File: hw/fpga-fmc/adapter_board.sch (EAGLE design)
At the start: 115 parts, among them IC1 M24C02, J1 5569262-1, J2 ASP-134488-01, U1 ADM3066E, U10 ADM3066E, U11 ADM3066E, U12 ADM3066E, U13 ADM3066E, U14 ADM3066E, U15 ADM3066E, U16 ADM3066E, U17 TCA9548A, U2 ADM3066E, U3 ADM3066E, U4 ADM3066E, U5 ADM3066E, U6 ADM3066E, U7 ADM3066E, U8 ADM3066E, U9 ADM3066E

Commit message: fpga-fmc: route right side
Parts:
- removed R54: (no value), rcl:R-EU_R0805
- added U$4: TXS0102, parts:TXS0102
- U$2: value TXS0104E -> TXS0102; device parts:TXS0104E -> parts:TXS0102
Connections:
- removed net N$13: R54.2, U$2.OE
- removed net N$2: U$2.A4
- removed net N$3: U$2.A3
- removed net N$4: U$2.A2
- removed net N$5: U$2.A1
- new net FMC_HA00_CC_N: J2E.F5, R23.2
- new net FMC_HA00_CC_P: J2E.F4, U2.DE, U2.RE
- new net FMC_HA01_CC_N: J2D.E3, U1.DE, U1.RE
- new net FMC_HA01_CC_P: J2D.E2, R2.2
- net 0V: now also U$4.GND; no longer R54.1
- net 1V8: now also U$4.VCCA
- net 5V: now also U$4.VCCB
- net CONV_OE: now also U$2.OE, U$4.OE
- net FMC_DP0_C2M_N: now also R25.2; no longer U1.DE, U1.RE
- net FMC_DP0_C2M_P: now also U3.DE, U3.RE; no longer R2.2
- net FMC_DP0_M2C_N: now also R29.2; no longer R27.2
- net FMC_DP0_M2C_P: now also U5.DE, U5.RE; no longer U4.DE, U4.RE
- net FMC_LA00_CC_N: now also R27.2; no longer R23.2
- net FMC_LA00_CC_P: now also U4.DE, U4.RE; no longer U2.DE, U2.RE
- net FMC_LA01_CC_N: now also R35.2; no longer R31.2
- net FMC_LA01_CC_P: now also U8.DE, U8.RE; no longer U6.DE, U6.RE
- net FMC_LA02_N: now also U$1.A1; no longer R25.2
- net FMC_LA02_P: now also U$1.A2; no longer U3.DE, U3.RE
- net FMC_LA03_N: now also U$3.A1; no longer R29.2
- net FMC_LA03_P: now also U$3.A2; no longer U5.DE, U5.RE
- net FMC_LA04_N: now also R31.2; no longer U$1.A1
- net FMC_LA04_P: now also U6.DE, U6.RE; no longer U$1.A2
- net FMC_LA05_N: now also R6.1, U17.SCL; no longer R35.2
- net FMC_LA05_P: now also R5.1, U17.SDA; no longer U8.DE, U8.RE
- net FMC_LA07_N: now also R51.2; no longer R39.2
- net FMC_LA07_P: now also U16.DE, U16.RE; no longer U10.DE, U10.RE
- net FMC_LA08_N: now also U$2.A1; no longer U$3.A1
- net FMC_LA08_P: now also U$2.A2; no longer U$3.A2
- net FMC_LA09_N: now also R39.2; no longer R37.2
- net FMC_LA09_P: now also U10.DE, U10.RE; no longer U9.DE, U9.RE
- net FMC_LA10_N: now also R37.2; no longer R6.1, U17.SCL
- net FMC_LA10_P: now also U9.DE, U9.RE; no longer R5.1, U17.SDA
- net FMC_LA11_N: now also R49.2; no longer R51.2
- net FMC_LA11_P: now also U15.DE, U15.RE; no longer U16.DE, U16.RE
- net FMC_LA12_N: now also U$4.A1; no longer R45.2
- net FMC_LA12_P: now also U$4.A2; no longer U13.DE, U13.RE
- net FMC_LA15_N: now also R47.2; no longer R49.2
- net FMC_LA15_P: now also U14.DE, U14.RE; no longer U15.DE, U15.RE
- net FMC_LA16_N: now also R45.2; no longer R47.2
- net FMC_LA16_P: now also U13.DE, U13.RE; no longer U14.DE, U14.RE
- net RJ1_CONV: now also U$4.B1; no longer U$2.B4
- net RJ5_CONV: now also U$4.B2; no longer U$2.B3

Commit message: hw/fpga-fmc: add 5V supply and route remaining CONV signals
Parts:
- added U$5: TSR1, parts:TSR1
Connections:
- net +12V: now also U$5.VIN; no longer J1.1.4, J1.2.4, J1.3.4, J1.4.4, J1.5.4, J1.6.4, J1.7.4, J1.8.4
- net 0V: now also U$5.GND+
- net 5V: now also J1.1.4, J1.2.4, J1.3.4, J1.4.4, J1.5.4, J1.6.4, J1.7.4, J1.8.4, U$5.VOUT
- net RJ1_CLK_N: now also R44.2, U13.B; no longer R48.2, U15.B
- net RJ1_CLK_P: now also R44.1, U13.A; no longer R48.1, U15.A
- net RJ1_DATA_N: now also R46.2, U14.B; no longer R50.2, U16.B
- net RJ1_DATA_P: now also R46.1, U14.A; no longer R50.1, U16.A
- net RJ2_CLK_N: now also R36.2, U9.B; no longer R40.2, U11.B
- net RJ2_CLK_P: now also R36.1, U9.A; no longer R40.1, U11.A
- net RJ2_DATA_N: now also R38.2, U10.B; no longer R42.2, U12.B
- net RJ2_DATA_P: now also R38.1, U10.A; no longer R42.1, U12.A
- net RJ5_CLK_N: now also R48.2, U15.B; no longer R44.2, U13.B
- net RJ5_CLK_P: now also R48.1, U15.A; no longer R44.1, U13.A
- net RJ5_DATA_N: now also R50.2, U16.B; no longer R46.2, U14.B
- net RJ5_DATA_P: now also R50.1, U16.A; no longer R46.1, U14.A
- net RJ6_CLK_N: now also R40.2, U11.B; no longer R36.2, U9.B
- net RJ6_CLK_P: now also R40.1, U11.A; no longer R36.1, U9.A
- net RJ6_DATA_N: now also R42.2, U12.B; no longer R38.2, U10.B
- net RJ6_DATA_P: now also R42.1, U12.A; no longer R38.1, U10.A

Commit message: hw/fpga-fmc: finalize pcb design and prepare BOM
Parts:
- removed U$5: TSR1, parts:TSR1
- added 12V_GOOD, 3V3_GOOD2, 5V_GOOD: (no value), led:LEDCHIPLED_0805
- added EESCL, EESDA, M_SCL, M_SDA, RJ1_CL+, RJ1_CL-, RJ1_CONV, RJ1_FC, RJ1_FCD, RJ1_FCL, RJ1_FDA, RJ1_FDA+, RJ1_FDA-, RJ1_FDD, RJ1_SCL, RJ1_SDO, RJ2_CONV, RJ2_FC, RJ2_FCD, RJ2_FCL, RJ2_FCL+, RJ2_FCL-, RJ2_FDA, RJ2_FDA+, RJ2_FDA-, RJ2_FDD, RJ2_SCL, RJ2_SDO, RJ3_CONV, RJ3_FC, RJ3_FCD, RJ3_FCL, RJ3_FCL+, RJ3_FCL-, RJ3_FDA, RJ3_FDA+, RJ3_FDA-, RJ3_FDD, RJ3_SCL, RJ3_SDO: TPB1,27, testpad:TPB1,27
- added J3, J4: (no value), pinhead:PINHD-1X3
- added R53: 330R, resistor:R-EU_R0805
- added R54: 1k, resistor:R-EU_R0805
- added R56: 130R, resistor:R-EU_R0805
- added R57, R58: 0R, rcl:R-EU_R0805
- added R59: NB, rcl:R-EU_R0805
- added X1: (no value), con-wago-508:W237-02P
- R1, R22, R24, R26, R28, R30, R32, R34, R36, R38, R40, R42, R44, R46, R48, R50: value (none) -> 120R
- R10, R11, R12, R13, R14, R15, R16, R17, R18, R19, R20, R21, R3, R4, R5, R6, R8, R9: value 1k -> 4k
- R55: value (none) -> 10k
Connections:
- new net FMC_HA05_N: J2D.E7, R59.1, U$1.A1
- new net N$2: 12V_GOOD.C, R54.2
- new net N$3: 3V3_GOOD2.C, R56.2
- new net N$5: 5V_GOOD.C, R53.2
- net +12V: now also 12V_GOOD.A, J3.2; no longer U$5.VIN
- net +3V3: now also 3V3_GOOD2.A, J3.1
- net 0V: now also J3.3, J4.3, R53.1, R54.1, R56.1, R59.2, X1-1.KL; no longer U$5.GND+
- net 1V8: now also J4.2
- net 1V8_POWER_GOOD: now also R58.1
- net 5V: now also 5V_GOOD.A, X1-2.KL; no longer U$5.VOUT
- net CONV_OE: now also R57.1, R58.2
- net FMC_IIC_SCL: now also EESCL.TP
- net FMC_IIC_SDA: now also EESDA.TP
- net FMC_LA01_CC_N: now also RJ3_FDA.TP
- net FMC_LA01_CC_P: now also RJ3_FDD.TP
- net FMC_LA02_N: now also R57.2; no longer U$1.A1
- net FMC_LA03_P: now also RJ3_FC.TP
- net FMC_LA05_N: now also M_SCL.TP
- net FMC_LA05_P: now also M_SDA.TP
- net FMC_LA06_N: now also RJ3_FCL.TP
- net FMC_LA06_P: now also RJ3_FCD.TP
- net FMC_LA08_N: now also RJ2_FC.TP
- net FMC_LA09_N: now also RJ2_FDA.TP
- net FMC_LA09_P: now also RJ2_FDD.TP
- net FMC_LA10_N: now also RJ2_FCL.TP
- net FMC_LA10_P: now also RJ2_FCD.TP
- net FMC_LA12_N: now also RJ1_FC.TP
- net FMC_LA15_N: now also RJ1_FDA.TP
- net FMC_LA15_P: now also RJ1_FDD.TP
- net FMC_LA16_N: now also RJ1_FCL.TP
- net FMC_LA16_P: now also RJ1_FCD.TP
- net RJ1_CLK_N: now also RJ1_CL-.TP
- net RJ1_CLK_P: now also RJ1_CL+.TP
- net RJ1_CONV: now also RJ1_CONV.TP
- net RJ1_DATA_N: now also RJ1_FDA-.TP
- net RJ1_DATA_P: now also RJ1_FDA+.TP
- net RJ1_SCL: now also RJ1_SCL.TP
- net RJ1_SDO: now also RJ1_SDO.TP
- net RJ2_CLK_N: now also RJ2_FCL-.TP
- net RJ2_CLK_P: now also RJ2_FCL+.TP
- net RJ2_CONV: now also RJ2_CONV.TP
- net RJ2_DATA_N: now also RJ2_FDA-.TP
- net RJ2_DATA_P: now also RJ2_FDA+.TP
- net RJ2_SCL: now also RJ2_SCL.TP
- net RJ2_SDO: now also RJ2_SDO.TP
- net RJ3_CLK_N: now also RJ3_FCL-.TP
- net RJ3_CLK_P: now also RJ3_FCL+.TP
- net RJ3_CONV: now also RJ3_CONV.TP
- net RJ3_DATA_N: now also RJ3_FDA-.TP
- net RJ3_DATA_P: now also RJ3_FDA+.TP
- net RJ3_SCL: now also RJ3_SCL.TP
- net RJ3_SDO: now also RJ3_SDO.TP
- net V+: now also J4.1
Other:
- moved on the sheet: C35, C36, C37

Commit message: hw/fpga-fmc: fix clearance issues
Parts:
- IC1: device parts:N24C02UDTG -> parts:N24C02UDTGSO8N
- R10, R11, R12, R13, R14, R15, R16, R17, R18, R19, R20, R21, R3, R4, R5, R6, R8, R9: value 4k -> 4.7k
- R52: value 0R -> NB
- renumbered 3V3_GOOD2 to 3V3_GOOD, U$1 to U18, U$2 to U20, U$3 to U19, U$4 to U21

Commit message: hw/fpga-fmc: fix connector turned by 180 degrees. add led for 1v8. change i2c package
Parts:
- added 1V8_GOOD: (no value), led:LEDCHIPLED_0805
- added R60: 10R, resistor:R-EU_R0805
- added R61: 10k, resistor:R-EU_R0805
- added R62: 130R, resistor:R-EU_R0805
- added U40: IRLML2502, parts:IRLML2502
- IC1: device parts:N24C02UDTGSO8N -> parts:N24C02UDTGTSSOP8
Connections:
- new net N$6: R60.1, R61.1, U40.G
- new net N$8: R62.2, U40.D
- new net N$9: 1V8_GOOD.C, R62.1
- net +3V3: now also 1V8_GOOD.A
- net 0V: now also R61.2, U40.S, X1-2.KL; no longer U17.A0, U17.A1, X1-1.KL
- net 1V8: now also R60.2
- net 5V: now also X1-1.KL; no longer X1-2.KL
- net FMC_IIC_SCL: now also M_SCL.TP, R6.1, U17.SCL
- net FMC_IIC_SDA: now also M_SDA.TP, R5.1, U17.SDA
- net FMC_LA05_N: no longer M_SCL.TP, R6.1, U17.SCL
- net FMC_LA05_P: no longer M_SDA.TP, R5.1, U17.SDA
- net GA0: now also U17.A1
- net GA1: now also U17.A0
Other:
- moved on the sheet: X1-1, X1-2

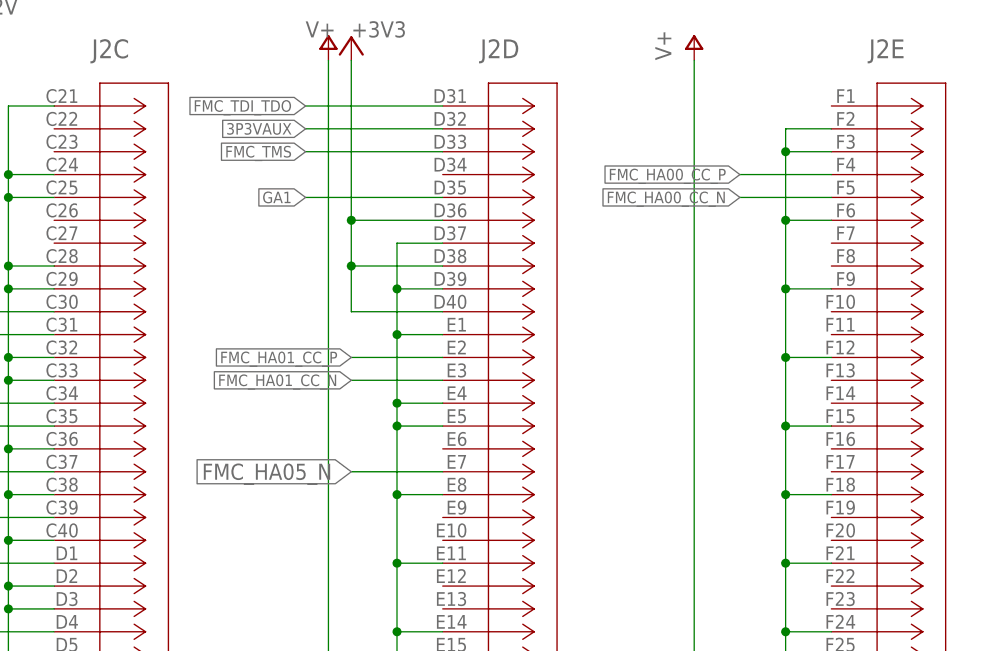
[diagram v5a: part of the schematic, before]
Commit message: hdl: copy all pin assignments to constraint file
note: RJ8 FMC connection are not connected on the FPGA board, so RJ8 cannot be used with the prototype pcb
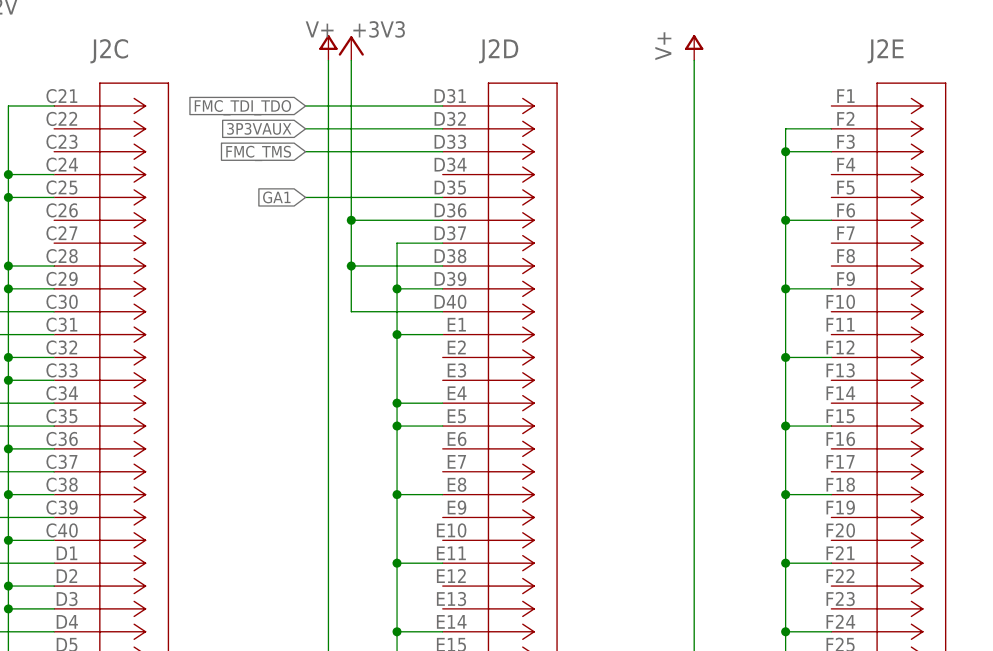
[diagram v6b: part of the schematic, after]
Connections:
- net FMC_HA00_CC_N: no longer J2E.F5
- net FMC_HA00_CC_P: no longer J2E.F4
- net FMC_HA01_CC_N: no longer J2D.E3
- net FMC_HA01_CC_P: no longer J2D.E2
- net FMC_HA05_N: no longer J2D.E7
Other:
- note added: "DO NOT CONNECT RJ8 TO HA PORTS!"
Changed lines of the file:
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@@
 <text x="1056.64" y="-25.4" size="1.778" layer="97">DATA IO 5</text>
 <text x="-279.4" y="104.14" size="1.27" layer="97">According to https://ohwr.org/project/ed/wikis/schematics-checklist#fmc-mezzanine-cards</text>
+<text x="-160.02" y="30.48" size="6.4516" layer="88">DO NOT CONNECT RJ8 TO HA PORTS!</text>
 </plain>
 <instances>
@@
 <net name="FMC_HA01_CC_P" class="0">
 <segment>
-<pinref part="J2" gate="D" pin="E2"/>
-<wire x1="-40.64" y1="287.02" x2="-50.8" y2="287.02" width="0.1524" layer="91"/>
-<label x="-50.8" y="287.02" size="1.27" layer="95" rot="R180" xref="yes"/>
-</segment>
-<segment>
 <pinref part="R2" gate="G$1" pin="2"/>
 <wire x1="149.86" y1="7.62" x2="147.32" y2="7.62" width="0.1524" layer="91"/>
@@
 <net name="FMC_HA01_CC_N" class="0">
 <segment>
-<pinref part="J2" gate="D" pin="E3"/>
-<wire x1="-40.64" y1="284.48" x2="-50.8" y2="284.48" width="0.1524" layer="91"/>
-<label x="-50.8" y="284.48" size="1.27" layer="95" rot="R180" xref="yes"/>
-</segment>
-<segment>
 <wire x1="154.94" y1="2.54" x2="147.32" y2="2.54" width="0.1524" layer="91"/>
 <pinref part="U1" gate="G$1" pin="DE"/>
@@
 <net name="FMC_HA00_CC_P" class="0">
 <segment>
-<pinref part="J2" gate="E" pin="F4"/>
-<wire x1="2.54" y1="307.34" x2="-7.62" y2="307.34" width="0.1524" layer="91"/>
-<label x="-7.62" y="307.34" size="1.27" layer="95" rot="R180" xref="yes"/>
-</segment>
-<segment>
 <wire x1="154.94" y1="-53.34" x2="147.32" y2="-53.34" width="0.1524" layer="91"/>
 <pinref part="U2" gate="G$1" pin="DE"/>
@@
 <net name="FMC_HA00_CC_N" class="0">
 <segment>
-<pinref part="J2" gate="E" pin="F5"/>
-<wire x1="2.54" y1="304.8" x2="-7.62" y2="304.8" width="0.1524" layer="91"/>
-<label x="-7.62" y="304.8" size="1.27" layer="95" rot="R180" xref="yes"/>
-</segment>
-<segment>
 <pinref part="R23" gate="G$1" pin="2"/>
 <wire x1="149.86" y1="-48.26" x2="147.32" y2="-48.26" width="0.1524" layer="91"/>
@@
 <net name="FMC_HA05_N" class="0">
 <segment>
-<pinref part="J2" gate="D" pin="E7"/>
-<wire x1="-40.64" y1="274.32" x2="-50.8" y2="274.32" width="0.1524" layer="91"/>
-<label x="-50.8" y="274.32" size="1.778" layer="95" rot="R180" xref="yes"/>
-</segment>
-<segment>
 <pinref part="U18" gate="G$1" pin="A1"/>

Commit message: turn FMC connector and reroute signals
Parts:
- added R63, R64: 0R, rcl:R-EU_R0805
- added R65, R66: 0R DNP, rcl:R-EU_R0805
- R57: value 0R -> 0R DNP
- R59: value NB -> DNP
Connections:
- removed net FMC_HA00_CC_N: R23.2
- removed net FMC_HA00_CC_P: U2.DE, U2.RE
- removed net FMC_HA01_CC_N: U1.DE, U1.RE
- removed net FMC_HA01_CC_P: R2.2
- removed net FMC_HA05_N: R59.1, U18.A1
- removed net I2C_RESET: R7.1, U17.RESET
- new net FMC_LA17_CC_N: J2C.D21
- new net FMC_LA17_CC_P: J2C.D20
- new net FMC_LA18_CC_N: J2C.C23
- new net FMC_LA18_CC_P: J2C.C22
- new net FMC_LA19_N: J2G.H23, RJ3_FC.TP, U19.A2
- new net FMC_LA19_P: J2G.H22, U19.A1
- new net FMC_LA20_N: J2F.G22
- new net FMC_LA20_P: J2F.G21
- new net FMC_LA21_N: J2G.H26, RJ3_FDD.TP, U8.DE, U8.RE
- new net FMC_LA21_P: J2G.H25, R35.2, RJ3_FDA.TP
- new net FMC_LA22_N: J2F.G25, R57.2
- new net FMC_LA22_P: J2F.G24, R7.1, U17.RESET
- new net FMC_LA23_N: J2C.D24
- new net FMC_LA23_P: J2C.D23
- new net FMC_LA24_N: J2G.H29, U6.DE, U6.RE
- new net FMC_LA24_P: J2G.H28, R31.2
- new net FMC_LA25_N: J2F.G28, RJ3_FCD.TP, U7.DE, U7.RE
- new net FMC_LA25_P: J2F.G27, R33.2, RJ3_FCL.TP
- new net FMC_LA26_N: J2C.D27
- new net FMC_LA26_P: J2C.D26
- new net FMC_LA27_N: J2C.C27
- new net FMC_LA27_P: J2C.C26
- new net FMC_LA28_N: J2G.H32, U5.DE, U5.RE
- new net FMC_LA28_P: J2G.H31, R29.2
- new net FMC_LA29_N: J2F.G31, U18.A2
- new net FMC_LA29_P: J2F.G30, R59.1, U18.A1
- new net FMC_LA30_N: J2G.H35, U4.DE, U4.RE
- new net FMC_LA30_P: J2G.H34, R27.2
- new net FMC_LA31_N: J2F.G34, R25.2
- new net FMC_LA31_P: J2F.G33, U3.DE, U3.RE
- new net FMC_LA32_N: J2G.H38, U2.DE, U2.RE
- new net FMC_LA32_P: J2G.H37, R23.2
- new net FMC_LA33_N: J2F.G37, U1.DE, U1.RE
- new net FMC_LA33_P: J2F.G36, R2.2
- new net I2C_SCL: M_SCL.TP, R6.1, R64.2, R66.1, U17.SCL
- new net I2C_SDA: M_SDA.TP, R5.1, R63.2, R65.1, U17.SDA
- net FMC_DP0_C2M_N: no longer R25.2
- net FMC_DP0_C2M_P: no longer U3.DE, U3.RE
- net FMC_DP0_M2C_N: no longer R29.2
- net FMC_DP0_M2C_P: no longer U5.DE, U5.RE
- net FMC_IIC_SCL: now also R64.1; no longer M_SCL.TP, R6.1, U17.SCL
- net FMC_IIC_SDA: now also R63.1; no longer M_SDA.TP, R5.1, U17.SDA
- net FMC_LA00_CC_N: now also RJ1_FCD.TP, U13.DE, U13.RE; no longer R27.2
- net FMC_LA00_CC_P: now also R45.2, RJ1_FCL.TP; no longer U4.DE, U4.RE
- net FMC_LA01_CC_N: now also R51.2; no longer R35.2, RJ3_FDA.TP
- net FMC_LA01_CC_P: now also U16.DE, U16.RE; no longer RJ3_FDD.TP, U8.DE, U8.RE
- net FMC_LA02_N: now also U21.A2; no longer R57.2
- net FMC_LA02_P: now also RJ1_FC.TP, U21.A1; no longer U18.A2
- net FMC_LA03_N: now also U12.DE, U12.RE; no longer U19.A1
- net FMC_LA03_P: now also R43.2; no longer RJ3_FC.TP, U19.A2
- net FMC_LA04_N: now also U11.DE, U11.RE; no longer R31.2
- net FMC_LA04_P: now also R41.2; no longer U6.DE, U6.RE
- net FMC_LA05_N: now also RJ1_FDD.TP, U14.DE, U14.RE
- net FMC_LA05_P: now also R47.2, RJ1_FDA.TP
- net FMC_LA06_N: now also U15.DE, U15.RE; no longer R33.2, RJ3_FCL.TP
- net FMC_LA06_P: now also R49.2; no longer RJ3_FCD.TP, U7.DE, U7.RE
- net FMC_LA07_N: now also RJ2_FDD.TP, U10.DE, U10.RE; no longer R51.2
- net FMC_LA07_P: now also R39.2, RJ2_FDA.TP; no longer U16.DE, U16.RE
- net FMC_LA08_N: no longer RJ2_FC.TP, U20.A1
- net FMC_LA08_P: no longer U20.A2
- net FMC_LA09_N: no longer R39.2, RJ2_FDA.TP
- net FMC_LA09_P: no longer RJ2_FDD.TP, U10.DE, U10.RE
- net FMC_LA10_N: no longer R37.2, RJ2_FCL.TP
- net FMC_LA10_P: no longer RJ2_FCD.TP, U9.DE, U9.RE
- net FMC_LA11_N: now also RJ2_FCD.TP, U9.DE, U9.RE; no longer R49.2
- net FMC_LA11_P: now also R37.2, RJ2_FCL.TP; no longer U15.DE, U15.RE
- net FMC_LA12_N: no longer RJ1_FC.TP, U21.A1
- net FMC_LA12_P: no longer U21.A2
- net FMC_LA13_N: no longer R43.2
- net FMC_LA13_P: no longer U12.DE, U12.RE
- net FMC_LA14_N: now also R65.2; no longer R41.2
- net FMC_LA14_P: now also R66.2; no longer U11.DE, U11.RE
- net FMC_LA15_N: now also U20.A2; no longer R47.2, RJ1_FDA.TP
- net FMC_LA15_P: now also RJ2_FC.TP, U20.A1; no longer RJ1_FDD.TP, U14.DE, U14.RE
- net FMC_LA16_N: no longer R45.2, RJ1_FCL.TP
- net FMC_LA16_P: no longer RJ1_FCD.TP, U13.DE, U13.RE
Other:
- note removed: "DO NOT CONNECT RJ8 TO HA PORTS!"
